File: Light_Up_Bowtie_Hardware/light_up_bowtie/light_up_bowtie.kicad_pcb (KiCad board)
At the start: 2 copper layers, 17 parts, among them SW1 SW_SPDT, U1 ATtiny85-20S

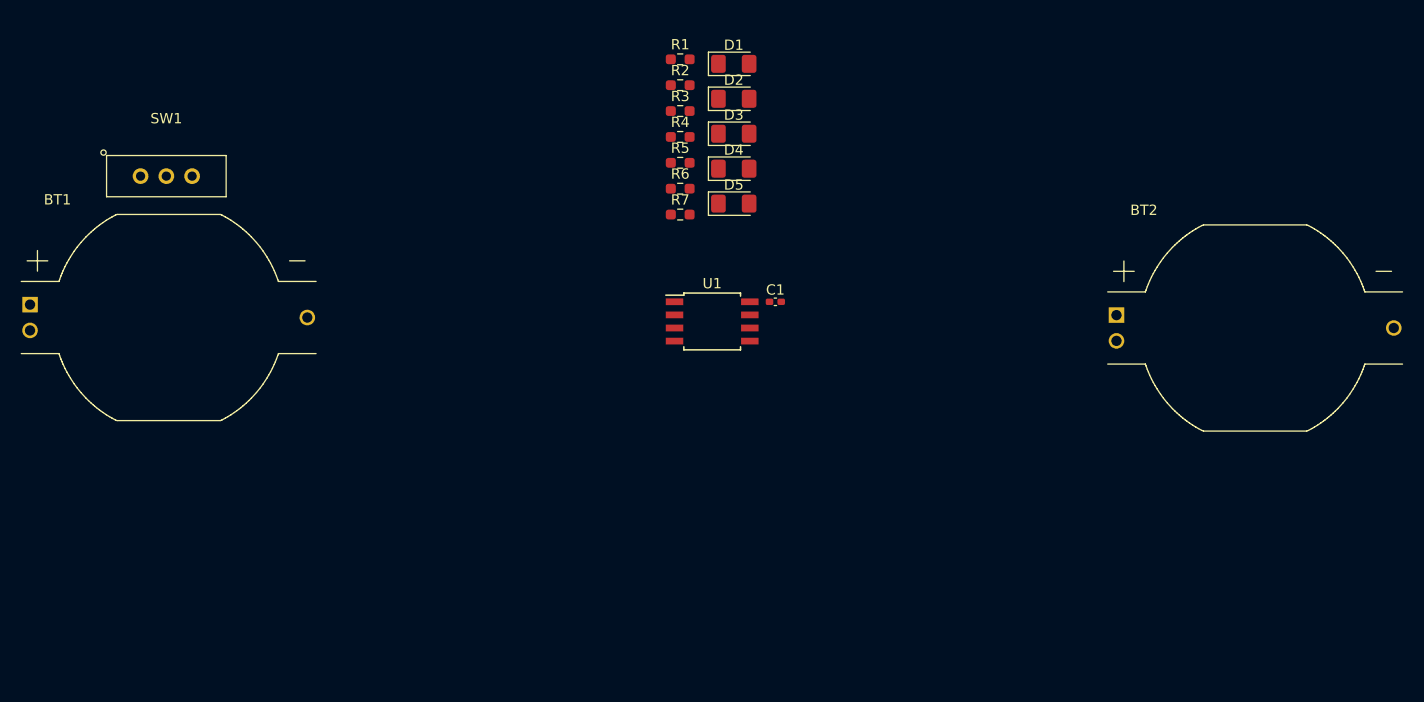
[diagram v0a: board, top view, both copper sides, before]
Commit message: Assigned footprints, added board shape, initial placement
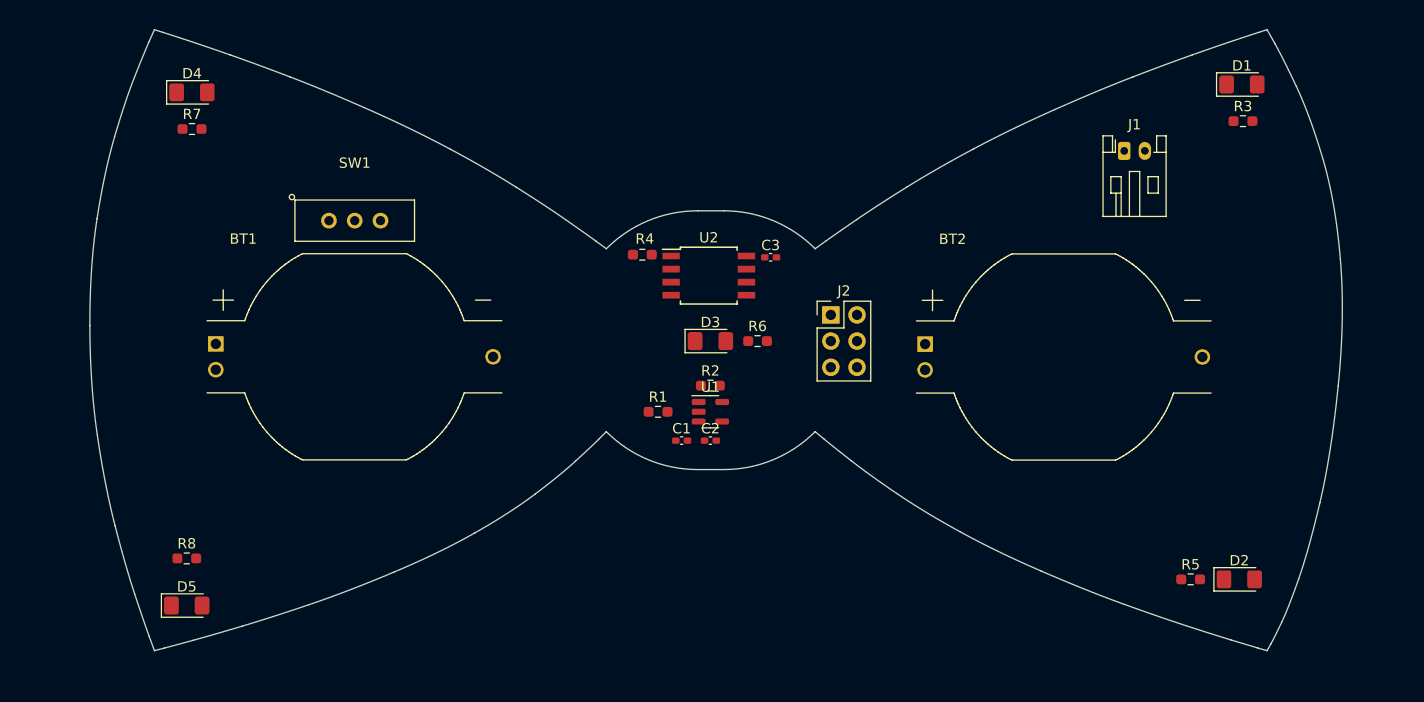
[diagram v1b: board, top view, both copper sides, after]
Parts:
- added C1: 1uF, Capacitor_SMD:C_0402_1005Metric_Pad0.74x0.62mm_HandSolder, F.Cu at (140.7, 115.3)
- added C3: 100nF, Capacitor_SMD:C_0402_1005Metric_Pad0.74x0.62mm_HandSolder, F.Cu at (149.4, 97.5)
- added J1: Conn_01x02, Connector_JST:JST_PH_S2B-PH-K_1x02_P2.00mm_Horizontal, F.Cu at (183.7, 87.2)
- added J2: Conn_02x03_Odd_Even, Connector_PinHeader_2.54mm:PinHeader_2x03_P2.54mm_Vertical, F.Cu at (155.2, 103.1)
- added R1: 10k, Resistor_SMD:R_0603_1608Metric_Pad0.98x0.95mm_HandSolder, F.Cu at (138.4, 112.5)
- added U1: AP2112K-3.3, Package_TO_SOT_SMD:SOT-23-5, F.Cu at (143.5, 112.5)
- C2: renamed from C1; value C -> 1uF
- moved D2 67.7 mm to (194.8, 128.8)
- moved D5 65.9 mm to (92.7, 131.3)
- moved R5 65.5 mm to (190.1, 128.8)
- moved R8 58.3 mm to (92.7, 126.7)
- moved R3 54.6 mm to (195.2, 84.3)
- moved D4 53.1 mm to (93.2, 81.5)
- moved D1 49.3 mm to (195.1, 80.8)
- moved R7 47.7 mm to (93.2, 85.1)
- moved R2 31.8 mm to (143.5, 110.0)
- moved D3 20.2 mm to (143.5, 105.7)
- moved R6 18.9 mm to (148.1, 105.7)
- moved SW1 18.8 mm to (109.0, 94.0)
- moved BT2 18.8 mm to (177.8, 107.2)
- moved BT1 18.4 mm to (109.0, 107.2)
- moved R4 16.8 mm to (136.9, 97.3)
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- renumbered R1 to R2, R2 to R4, R4 to R5, R5 to R6, R6 to R7, R7 to R8, U1 to U2
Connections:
- C2 pad 1: Net-(SW1-C) -> Net-(J2-Pin_2)
- R2 pad 2: Net-(U1-VCC) -> Net-(J2-Pin_2)
- R4 pad 1: Net-(U1-VCC) -> Net-(J2-Pin_2)
- U2 pad 8: Net-(U1-VCC) -> Net-(J2-Pin_2)
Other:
- board outline added: 121.5 x 60.2 mm

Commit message: Finished placement, added constraints
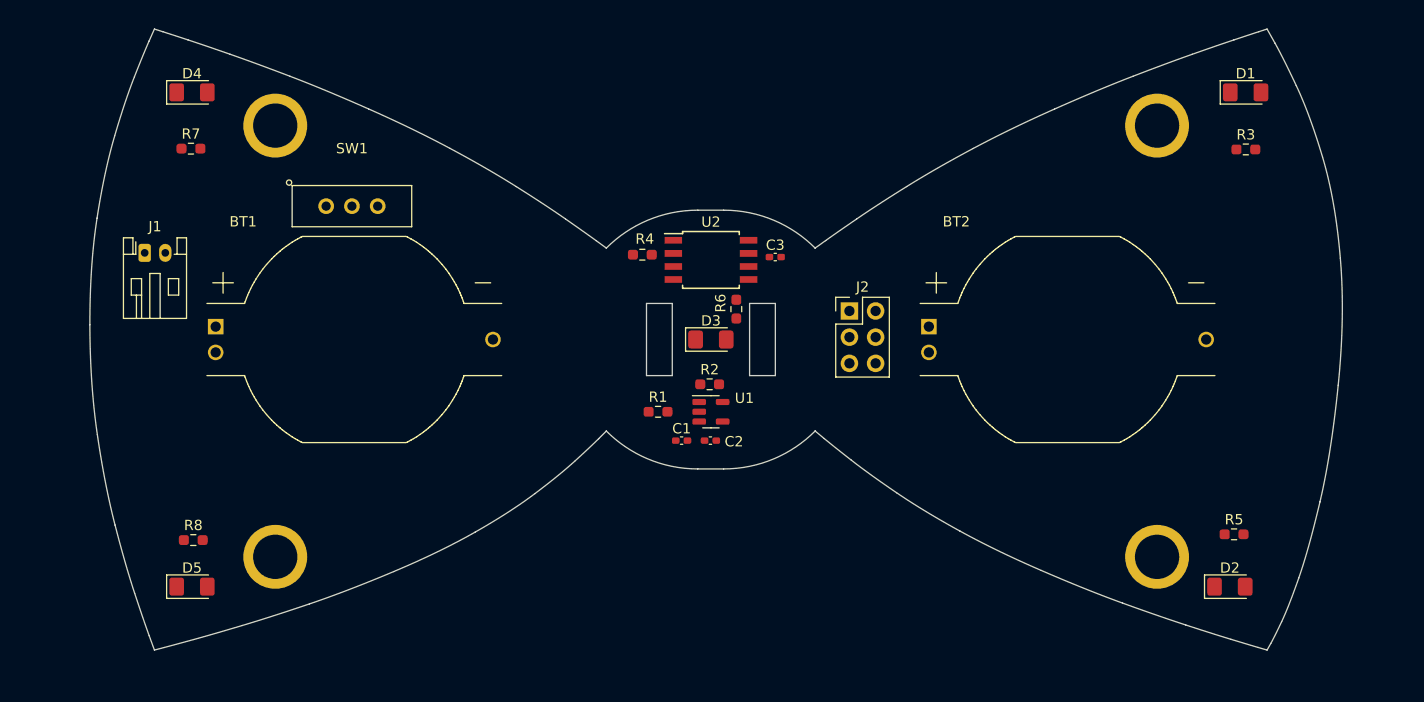
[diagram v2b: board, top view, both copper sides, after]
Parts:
- added REF**: MountingHole_4.3mm_M4_ISO14580_Pad, MountingHole:MountingHole_4.3mm_M4_ISO14580_Pad, F.Cu at (186.8, 84.8)
- added REF**: MountingHole_4.3mm_M4_ISO14580_Pad, MountingHole:MountingHole_4.3mm_M4_ISO14580_Pad, F.Cu at (101.3, 126.6)
- added REF**: MountingHole_4.3mm_M4_ISO14580_Pad, MountingHole:MountingHole_4.3mm_M4_ISO14580_Pad, F.Cu at (101.3, 84.8)
- added REF**: MountingHole_4.3mm_M4_ISO14580_Pad, MountingHole:MountingHole_4.3mm_M4_ISO14580_Pad, F.Cu at (186.8, 126.6)
- moved J1 95.5 mm to (88.6, 97.1)
- moved R5 6.07 mm to (194.3, 124.4)
- moved R6 3.72 mm to (146.0, 102.6), turned to -90 degrees
- moved R3 2.76 mm to (195.5, 87.1)
- moved R7 1.91 mm to (93.1, 87.0)
- moved D5 1.90 mm to (93.2, 129.5)
- moved R8 1.89 mm to (93.3, 125.0)
- moved J2 1.84 mm to (157.0, 102.7)
- moved BT2 1.74 mm to (178.2, 105.5)
- moved BT1 1.68 mm to (109.0, 105.5)
- moved U2 1.54 mm to (143.6, 97.8)
- moved SW1 1.43 mm to (108.7, 92.6)
- moved D2 1.16 mm to (193.9, 129.5)
- moved D1 0.84 mm to (195.4, 81.5)
- moved C3 0.45 mm to (149.8, 97.5)
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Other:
- outline, holes or cut-outs redrawn

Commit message: layout completed
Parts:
- moved D1 112.9 mm to (93.2, 129.5)
- moved D2 111.5 mm to (93.2, 81.5)
- moved R3 108.6 mm to (93.8, 125.2)
- moved R5 107.3 mm to (93.8, 86.9)
- moved R7 102.5 mm to (195.6, 86.5)
- moved D4 102.2 mm to (195.4, 81.5)
- moved D5 102.2 mm to (195.4, 129.5)
- moved R8 102.2 mm to (195.5, 124.9)
- moved C2 18.0 mm to (146.5, 97.6), turned to -90 degrees
- moved C1 17.7 mm to (140.9, 97.6), turned to -90 degrees
- moved R4 15.5 mm to (151.9, 101.0), turned to 90 degrees
- moved U2 15.2 mm to (143.6, 113.0)
- moved R1 14.5 mm to (138.4, 98.0)
- moved U1 14.5 mm to (143.6, 98.0)
- moved R2 14.5 mm to (143.6, 95.4)
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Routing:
- net Net-(J2-Pin_1): track 0.00 -> 78.1 mm, vias 0 -> 2
- net Net-(U2-XTAL1/PB3): track 0.00 -> 76.7 mm
- net Net-(J2-Pin_4): track 0.00 -> 62.1 mm
- net Net-(U2-XTAL2/PB4): track 0.00 -> 58.7 mm
- net Net-(BT1-Pad3): track 0.00 -> 49.3 mm, vias 0 -> 1
- net Net-(J2-Pin_2): track 0.00 -> 40.5 mm, vias 0 -> 2
- net Net-(SW1-C): track 0.00 -> 35.6 mm
- net VCC: track 0.00 -> 34.5 mm
- net Net-(J2-Pin_5): track 0.00 -> 31.5 mm, vias 0 -> 2
- net Net-(J2-Pin_3): track 0.00 -> 18.5 mm
- net GND: track 0.00 -> 5.80 mm, vias 0 -> 1
- net Net-(D2-A): track 0.00 -> 5.34 mm
- net Net-(D4-A): track 0.00 -> 5.10 mm
- net Net-(D5-A): track 0.00 -> 4.79 mm
- net Net-(D1-A): track 0.00 -> 4.25 mm
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- added copper zone on B.Cu, net GND
- added copper zone on F.Cu, net GND
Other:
- board text added: "Greg's Builds 2024"
- board text added: "v01"
